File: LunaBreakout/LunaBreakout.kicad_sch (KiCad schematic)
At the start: 1 part, among them U1 STM32G0B1RBTx

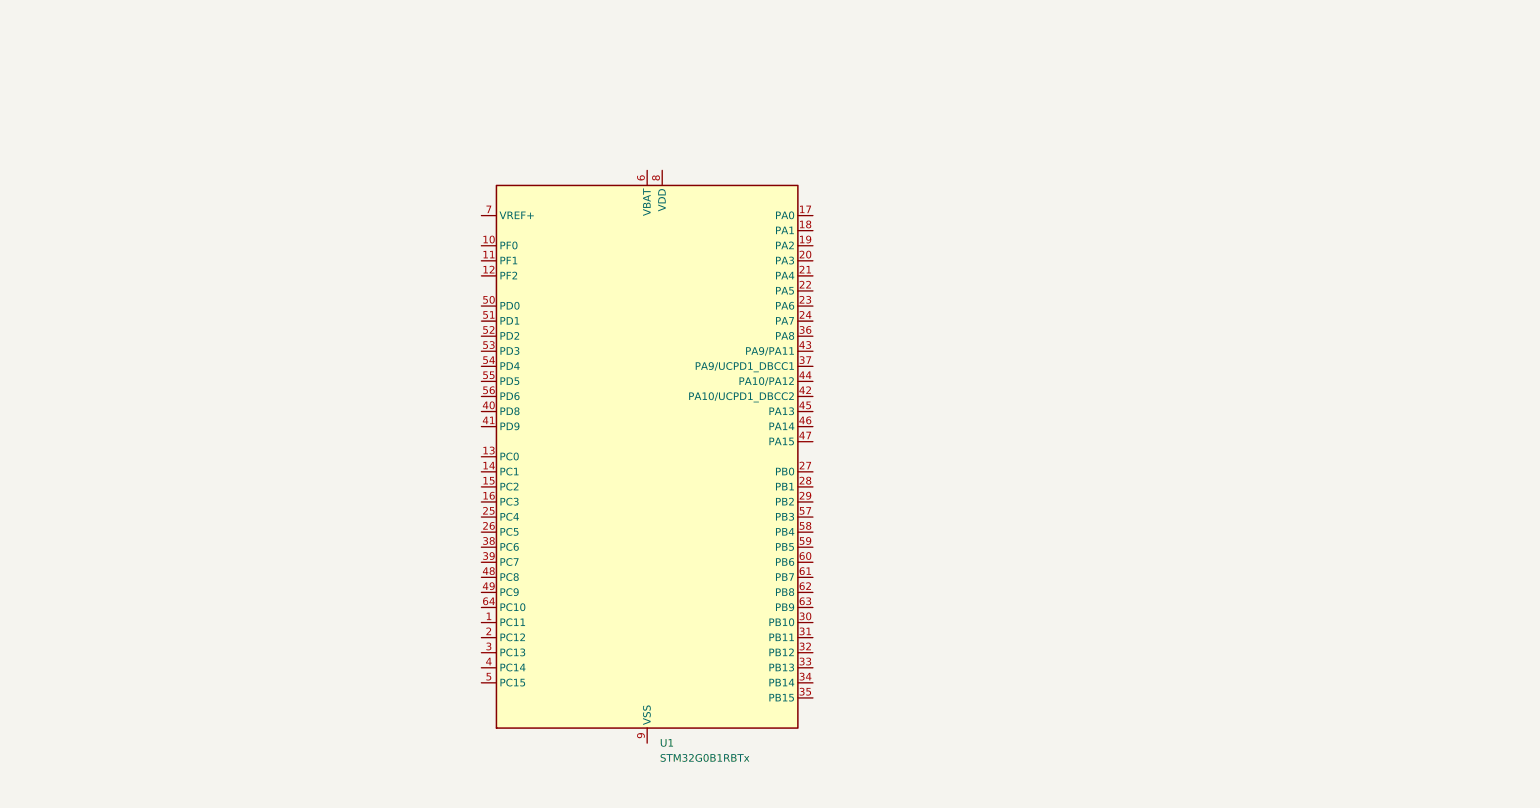
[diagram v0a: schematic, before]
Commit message: Added USBC & voltage regulator
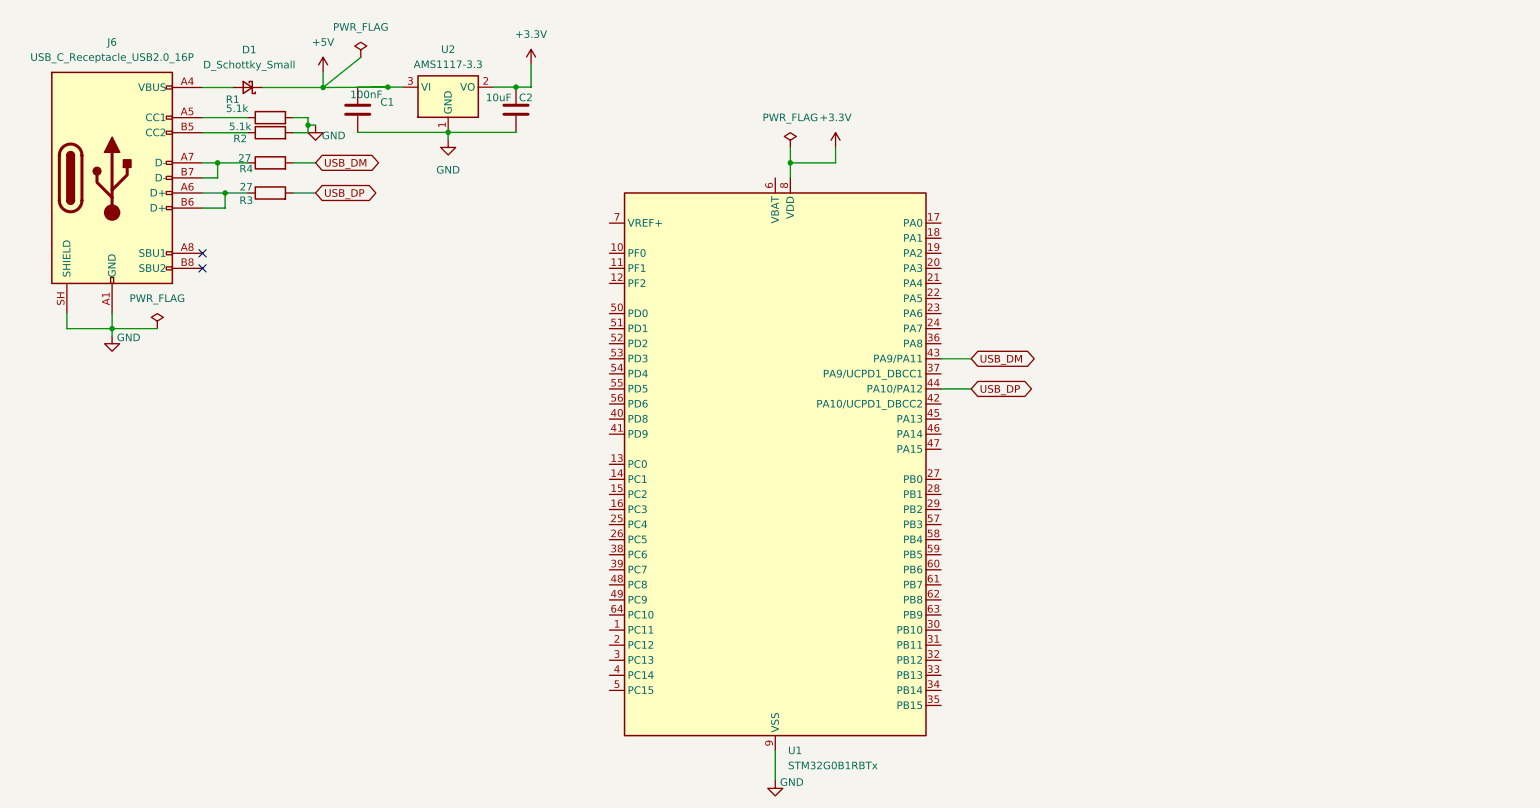
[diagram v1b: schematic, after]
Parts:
- added C1: 100nF, Capacitor_SMD:C_0805_2012Metric, symbol Device:C
- added C2: 10uF, Capacitor_SMD:C_0805_2012Metric, symbol Device:C
- added D1: D_Schottky_Small, Diode_SMD:D_SMA, symbol Device:D_Schottky_Small
- added J6: USB_C_Receptacle_USB2.0_16P, Connector_USB:USB_C_Receptacle_HRO_TYPE-C-31-M-12, symbol Connector:USB_C_Receptacle_USB2.0_16P
- added R1, R2: 5.1k, Resistor_SMD:R_0805_2012Metric, symbol Device:R
- added R3, R4: 27, Resistor_SMD:R_0805_2012Metric, symbol Device:R
- added U2: AMS1117-3.3, Package_TO_SOT_SMD:SOT-223-3_TabPin2, symbol Regulator_Linear:AMS1117-3.3
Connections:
- net USB_DM: now reaches U1.43 (PA9/PA11)
- net USB_DM: now also R4.2
- net USB_DP: now reaches U1.44 (PA10/PA12)
- net USB_DP: now also R3.2
- net +3.3V: now reaches U1.8 (VDD)
- net +3.3V: now also C2.1, U2.2 (VO)
- net GND: now reaches U1.9 (VSS)
- net GND: now also C1.2, C2.2, J6.A1 (GND), J6.A12 (GND), J6.B1 (GND), J6.B12 (GND), J6.SH (SHIELD), R1.2, R2.2, U2.1 (GND)
- new net: D1.2 (A), J6.A4 (VBUS), J6.A9 (VBUS), J6.B4 (VBUS), J6.B9 (VBUS)
- new net: J6.A5 (CC1), R1.1
- new net: J6.A6 (D+), J6.B6 (D+), R3.1
- new net: J6.A7 (D-), J6.B7 (D-), R4.1
- new net: J6.B5 (CC2), R2.1
- new net +5V: C1.1, D1.1 (K), U2.3 (VI)
- no-connect marks 0 -> 2

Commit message: Added reset and boot buttons
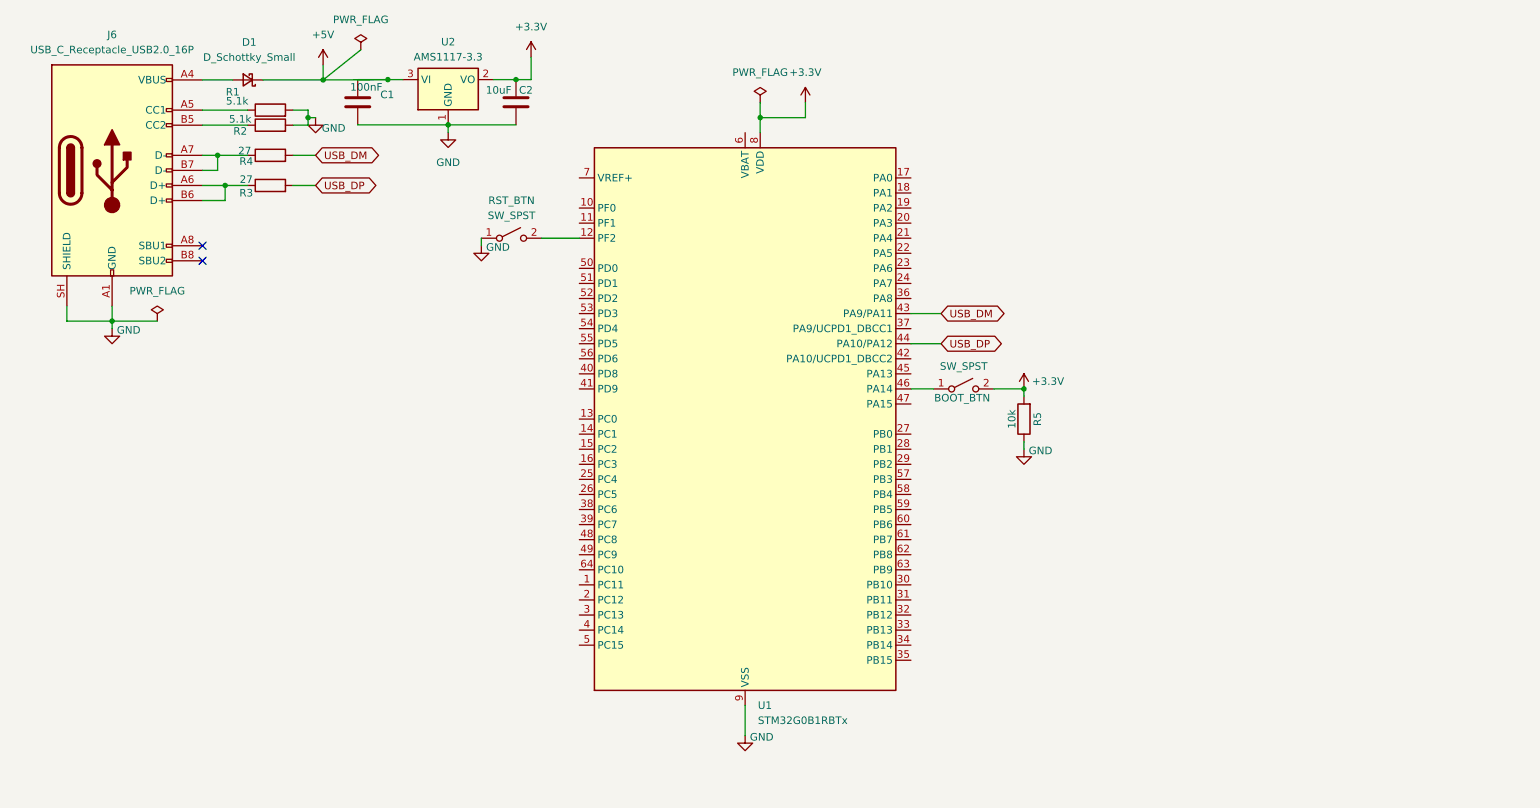
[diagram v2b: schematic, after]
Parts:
- added BOOT_BTN, RST_BTN: SW_SPST, Button_Switch_SMD:SW_SPST_CK_RS282G05A3, symbol Switch:SW_SPST
- added R5: 10k, Resistor_SMD:R_0805_2012Metric, symbol Device:R
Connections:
- net +3.3V: now also BOOT_BTN.2 (B), R5.2
- net GND: now also R5.1, RST_BTN.1 (A)
- net at U1.12 (PF2): now also RST_BTN.2 (B)
- net at U1.46 (PA14): now also BOOT_BTN.1 (A)

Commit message: Switched to RP2040
Added, CAN chip & connector, UART connector with isolator, I2C connector
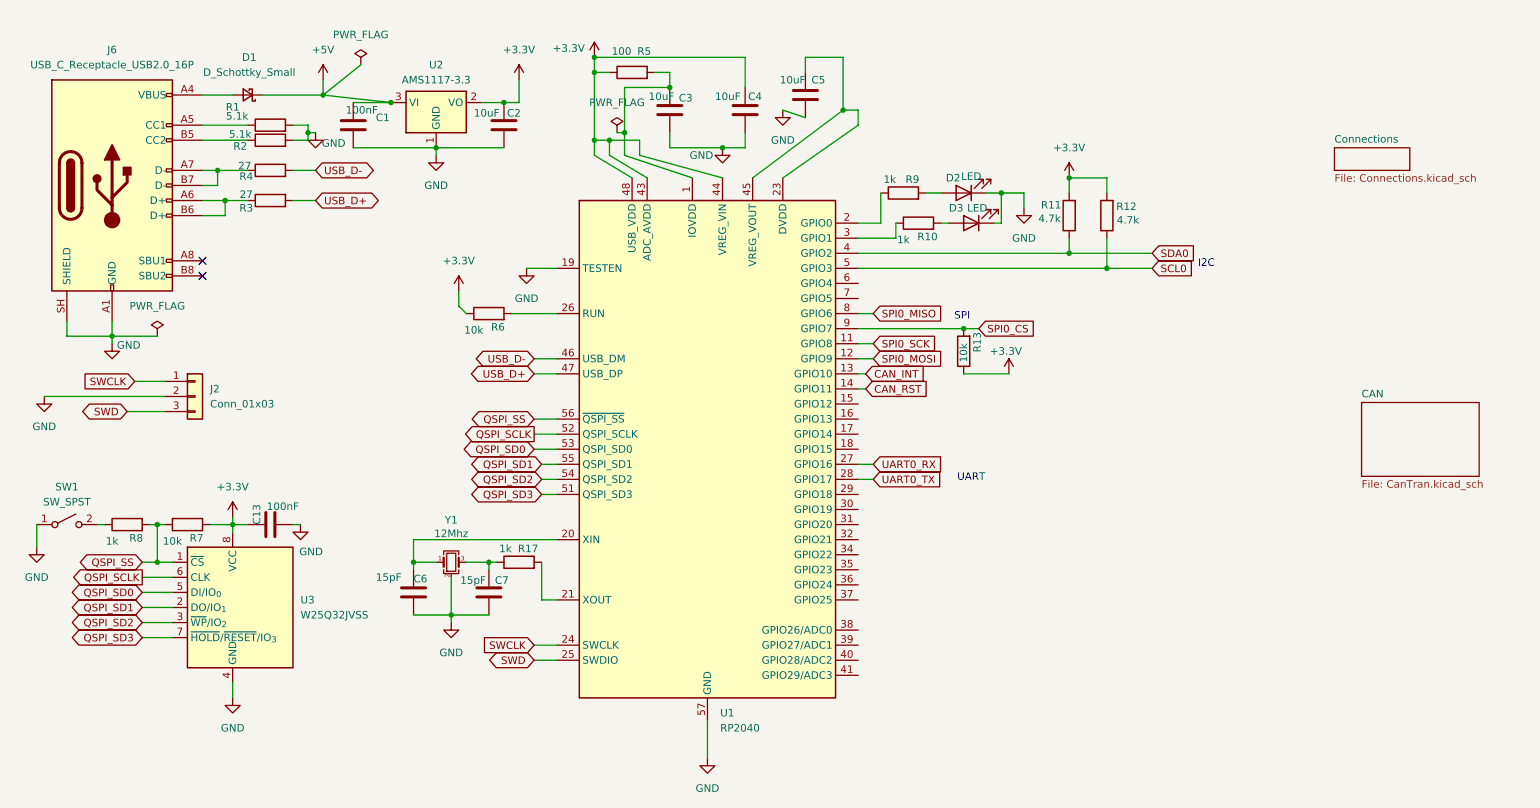
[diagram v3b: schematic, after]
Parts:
- removed BOOT_BTN, RST_BTN: SW_SPST, Button_Switch_SMD:SW_SPST_CK_RS282G05A3, symbol Switch:SW_SPST
- removed U1: STM32G0B1RBTx, Package_QFP:LQFP-64_10x10mm_P0.5mm, symbol MCU_ST_STM32G0:STM32G0B1RBTx
- added C13: 100nF, Capacitor_SMD:C_0805_2012Metric, symbol Device:C
- added C3, C4, C5: 10uF, Capacitor_SMD:C_0805_2012Metric, symbol Device:C
- added C6, C7: 15pF, Capacitor_SMD:C_0805_2012Metric, symbol Device:C
- added D2, D3: LED, LED_SMD:LED_0805_2012Metric, symbol Device:LED
- added J2: Conn_01x03, Connector_PinSocket_2.54mm:PinSocket_1x03_P2.54mm_Vertical, symbol Connector_Generic:Conn_01x03
- added R10, R17, R8, R9: 1k, Resistor_SMD:R_0805_2012Metric, symbol Device:R
- added R11, R12: 4.7k, Resistor_SMD:R_0805_2012Metric, symbol Device:R
- added R13, R6, R7: 10k, Resistor_SMD:R_0805_2012Metric, symbol Device:R
- added SW1: SW_SPST, Button_Switch_SMD:SW_SPST_CK_RS282G05A3, symbol Switch:SW_SPST
- added U1: RP2040, Package_DFN_QFN:QFN-56-1EP_7x7mm_P0.4mm_EP3.2x3.2mm, symbol MCU_RaspberryPi:RP2040
- added U3: W25Q32JVSS, Package_SON:WSON-8-1EP_4x4mm_P0.8mm_EP2.2x3mm, symbol Memory_Flash:W25Q32JVSS
- added Y1: 12Mhz, Crystal:Crystal_SMD_SeikoEpson_FA238V-4Pin_3.2x2.5mm, symbol Device:Crystal_GND24_Small
- J6: footprint Connector_USB:USB_C_Receptacle_HRO_TYPE-C-31-M-12 -> Connector_USB:USB_C_Receptacle_XKB_U262-16XN-4BVC11
- R5: value 10k -> 100
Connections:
- net +3.3V: now also R5.1, C13.1, C4.1, R11.2, R12.2, R13.1, R6.1, R7.2, U1.43 (ADC_AVDD), U1.44 (VREG_VIN), U1.48 (USB_VDD), U3.8 (VCC); no longer R5.2
- net GND: now also C13.2, C3.2, C4.2, C5.2, C6.2, C7.2, D2.1 (K), D3.1 (K), J2.2 (Pin_2), SW1.1 (A), U1.19 (TESTEN), U1.57 (GND), U3.4 (GND), Y1.2 (G), Y1.4 (G); no longer R5.1
- net USB_DM renamed USB_D-
- net USB_D-: now also U1.46 (USB_DM)
- net USB_DP renamed USB_D+
- net USB_D+: now also U1.47 (USB_DP)
- new net: R8.1, SW1.2 (B)
- new net: R6.2, U1.26 (RUN)
- new net: D3.2 (A), R10.2
- new net: D2.2 (A), R9.2
- new net: C5.1, U1.23 (DVDD), U1.45 (VREG_VOUT), U1.50 (DVDD)
- new net: C3.1, R5.2, U1.1 (IOVDD), U1.10 (IOVDD), U1.22 (IOVDD), U1.33 (IOVDD), U1.42 (IOVDD), U1.49 (IOVDD)
- new net: R10.1, U1.3 (GPIO1)
- new net: C7.1, R17.1, Y1.3
- new net: R17.2, U1.21 (XOUT)
- new net: R9.1, U1.2 (GPIO0)
- new net: C6.1, U1.20 (XIN), Y1.1
- new net CAN_INT: U1.13 (GPIO10)
- new net CAN_RST: U1.14 (GPIO11)
- new net QSPI_SCLK: U1.52 (QSPI_SCLK), U3.6 (CLK)
- new net QSPI_SD0: U1.53 (QSPI_SD0), U3.5 (DI/IO_{0})
- new net QSPI_SD1: U1.55 (QSPI_SD1), U3.2 (DO/IO_{1})
- new net QSPI_SD2: U1.54 (QSPI_SD2), U3.3 (~{WP}/IO_{2})
- new net QSPI_SD3: U1.51 (QSPI_SD3), U3.7 (~{HOLD}/~{RESET}/IO_{3})
- new net QSPI_SS: R7.1, R8.2, U1.56 (~{QSPI_SS}), U3.1 (~{CS})
- new net SCL0: R12.1, U1.5 (GPIO3)
- new net SDA0: R11.1, U1.4 (GPIO2)
- new net SPI0_CS: R13.2, U1.9 (GPIO7)
- new net SPI0_MISO: U1.8 (GPIO6)
- new net SPI0_MOSI: U1.12 (GPIO9)
- new net SPI0_SCK: U1.11 (GPIO8)
- new net SWCLK: J2.1 (Pin_1), U1.24 (SWCLK)
- new net SWD: J2.3 (Pin_3), U1.25 (SWDIO)
- new net UART0_RX: U1.27 (GPIO16)
- new net UART0_TX: U1.28 (GPIO17)
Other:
- added sheet CAN (CanTran.kicad_sch)
- added sheet Connections (Connections.kicad_sch)
- note added: "I2C"
- note added: "SPI"
- note added: "UART"

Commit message: changed debug header to jst
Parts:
- J2: footprint Connector_PinSocket_2.54mm:PinSocket_1x03_P2.54mm_Vertical -> Connector_JST:JST_XH_B3B-XH-A_1x03_P2.50mm_Vertical
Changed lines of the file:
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@@
 			)
 		)
-		(property "Footprint" "Connector_PinSocket_2.54mm:PinSocket_1x03_P2.54mm_Vertical"
+		(property "Footprint" "Connector_JST:JST_XH_B3B-XH-A_1x03_P2.50mm_Vertical"
 			(at 41.91 78.74 0)
 			(hide yes)

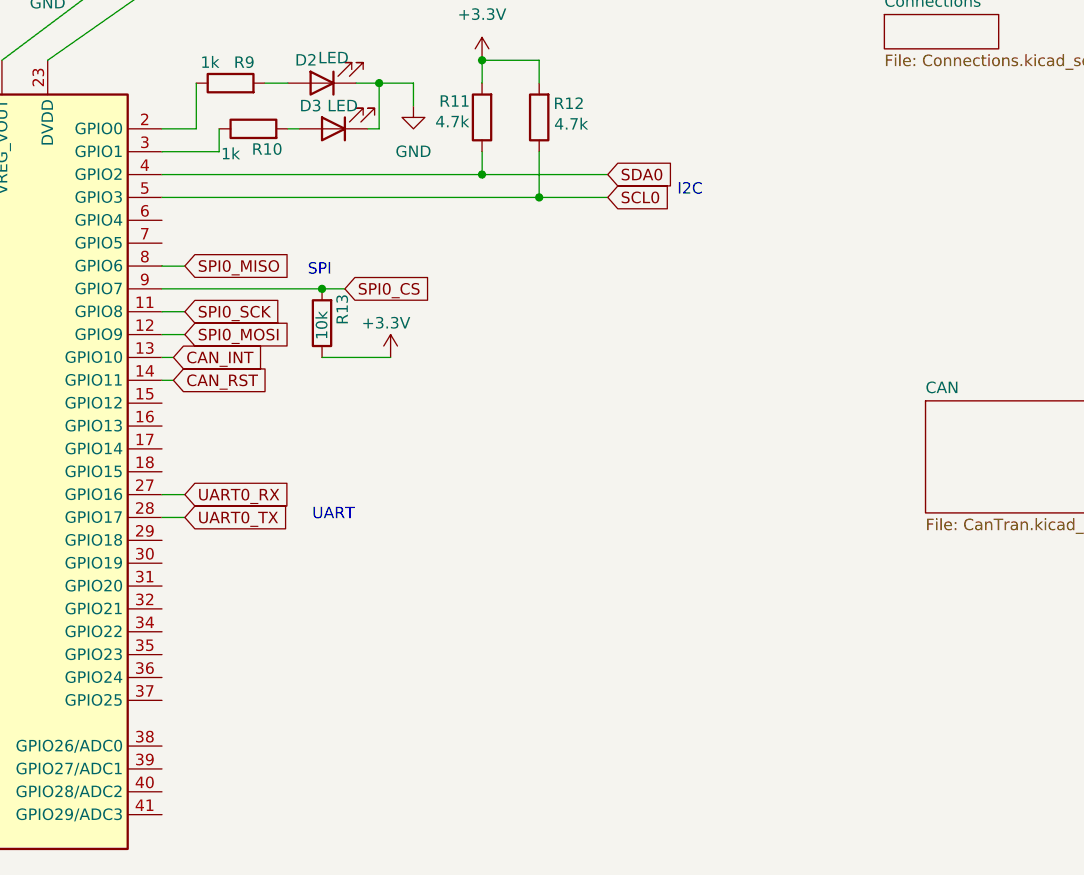
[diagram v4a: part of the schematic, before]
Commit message: Fixed net labels, added connectors for the communication ports added
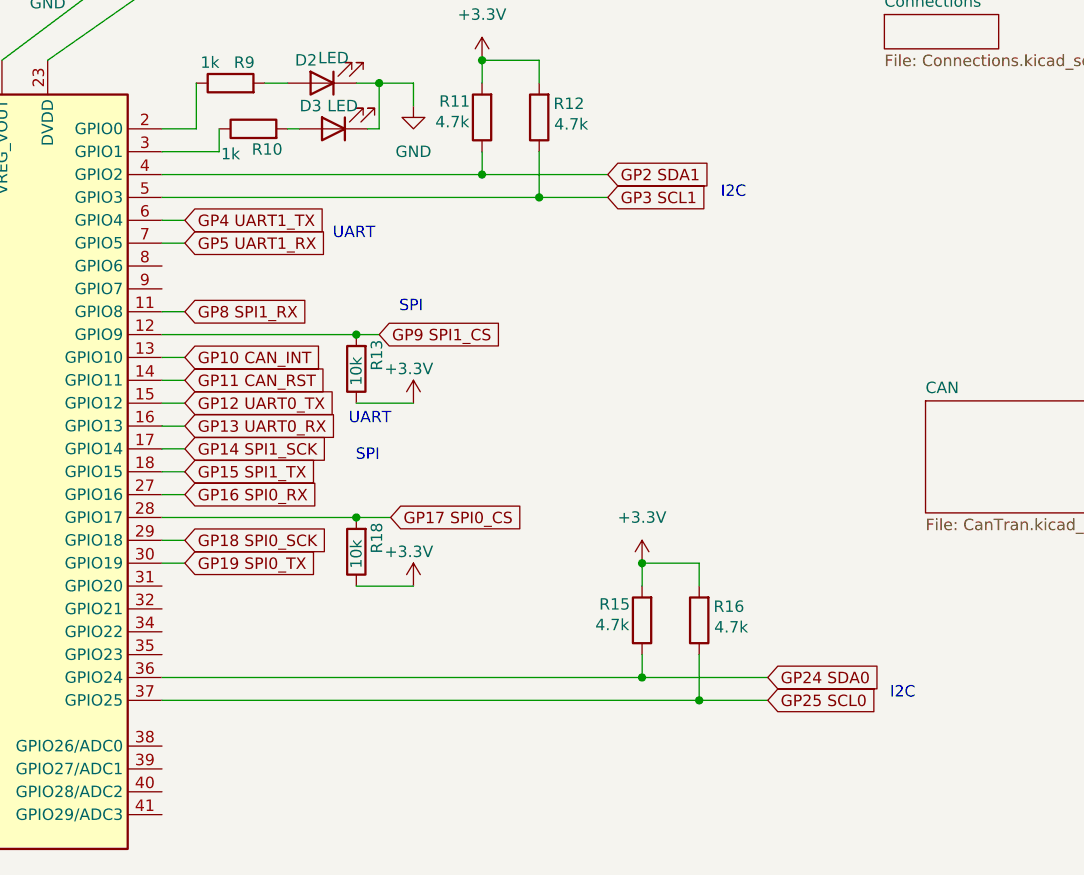
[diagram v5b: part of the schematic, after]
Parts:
- added R15, R16: 4.7k, Resistor_SMD:R_0805_2012Metric, symbol Device:R
- added R18: 10k, Resistor_SMD:R_0805_2012Metric, symbol Device:R
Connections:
- net +3.3V: now also R15.2, R16.2, R18.1
- net GP12 UART0_TX: now reaches U1.15 (GPIO12)
- net GP13 UART0_RX: now reaches U1.16 (GPIO13)
- net GP14 SPI1_SCK: now reaches U1.17 (GPIO14)
- net GP15 SPI1_TX: now reaches U1.18 (GPIO15)
- net GP18 SPI0_SCK: now reaches U1.29 (GPIO18)
- net GP19 SPI0_TX: now reaches U1.30 (GPIO19)
- net GP24 SDA0: now reaches U1.36 (GPIO24)
- net GP24 SDA0: now also R15.1
- net GP25 SCL0: now reaches U1.37 (GPIO25)
- net GP25 SCL0: now also R16.1
- net GP4 UART1_TX: now reaches U1.6 (GPIO4)
- net GP5 UART1_RX: now reaches U1.7 (GPIO5)
- net CAN_INT renamed GP10 CAN_INT
- net CAN_RST renamed GP11 CAN_RST
- net SCL0 renamed GP3 SCL1
- net SDA0 renamed GP2 SDA1
- net SPI0_CS: no longer names the net of U1.9 (GPIO7)
- net SPI0_CS: no longer R13.2
- net SPI0_MISO: no longer names the net of U1.8 (GPIO6)
- net SPI0_MOSI renamed GP9 SPI1_CS
- net GP9 SPI1_CS: now also R13.2
- net SPI0_SCK renamed GP8 SPI1_RX
- net UART0_RX renamed GP16 SPI0_RX
- net UART0_TX renamed GP17 SPI0_CS
- net GP17 SPI0_CS: now also R18.2
